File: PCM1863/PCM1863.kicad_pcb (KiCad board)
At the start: 2 copper layers, 86 parts, among them IC1 SN74AUC1G126DCKR, IC2 NCP163ASN330T1G, IC3 NCP163ASN330T1G, IC4 TXB0101DBVT, J1 Conn_01x10_Male, J2 Conn_01x10_Male, J3 Conn_01x10_Male, J4 USB_B_Micro, U1 PCM1863, Y1 ASE-24.000MHZ-ET, Y2 ASE-22.000MHZ-ET

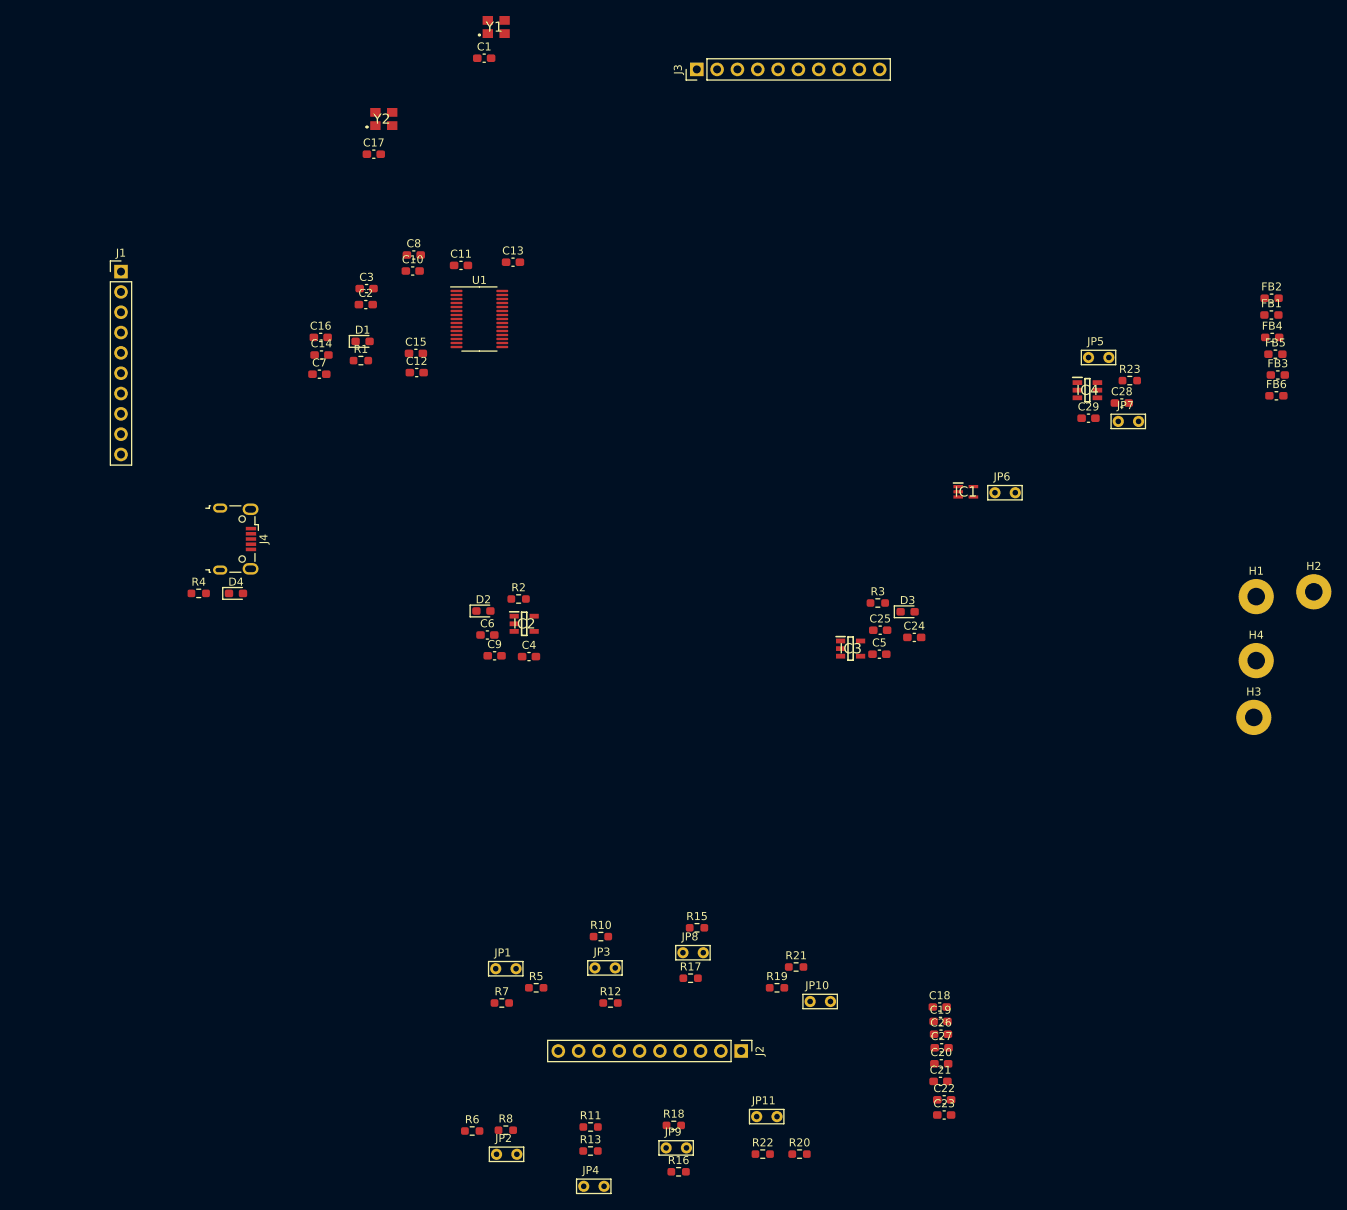
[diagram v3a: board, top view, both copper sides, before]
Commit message: finished ADC v.4
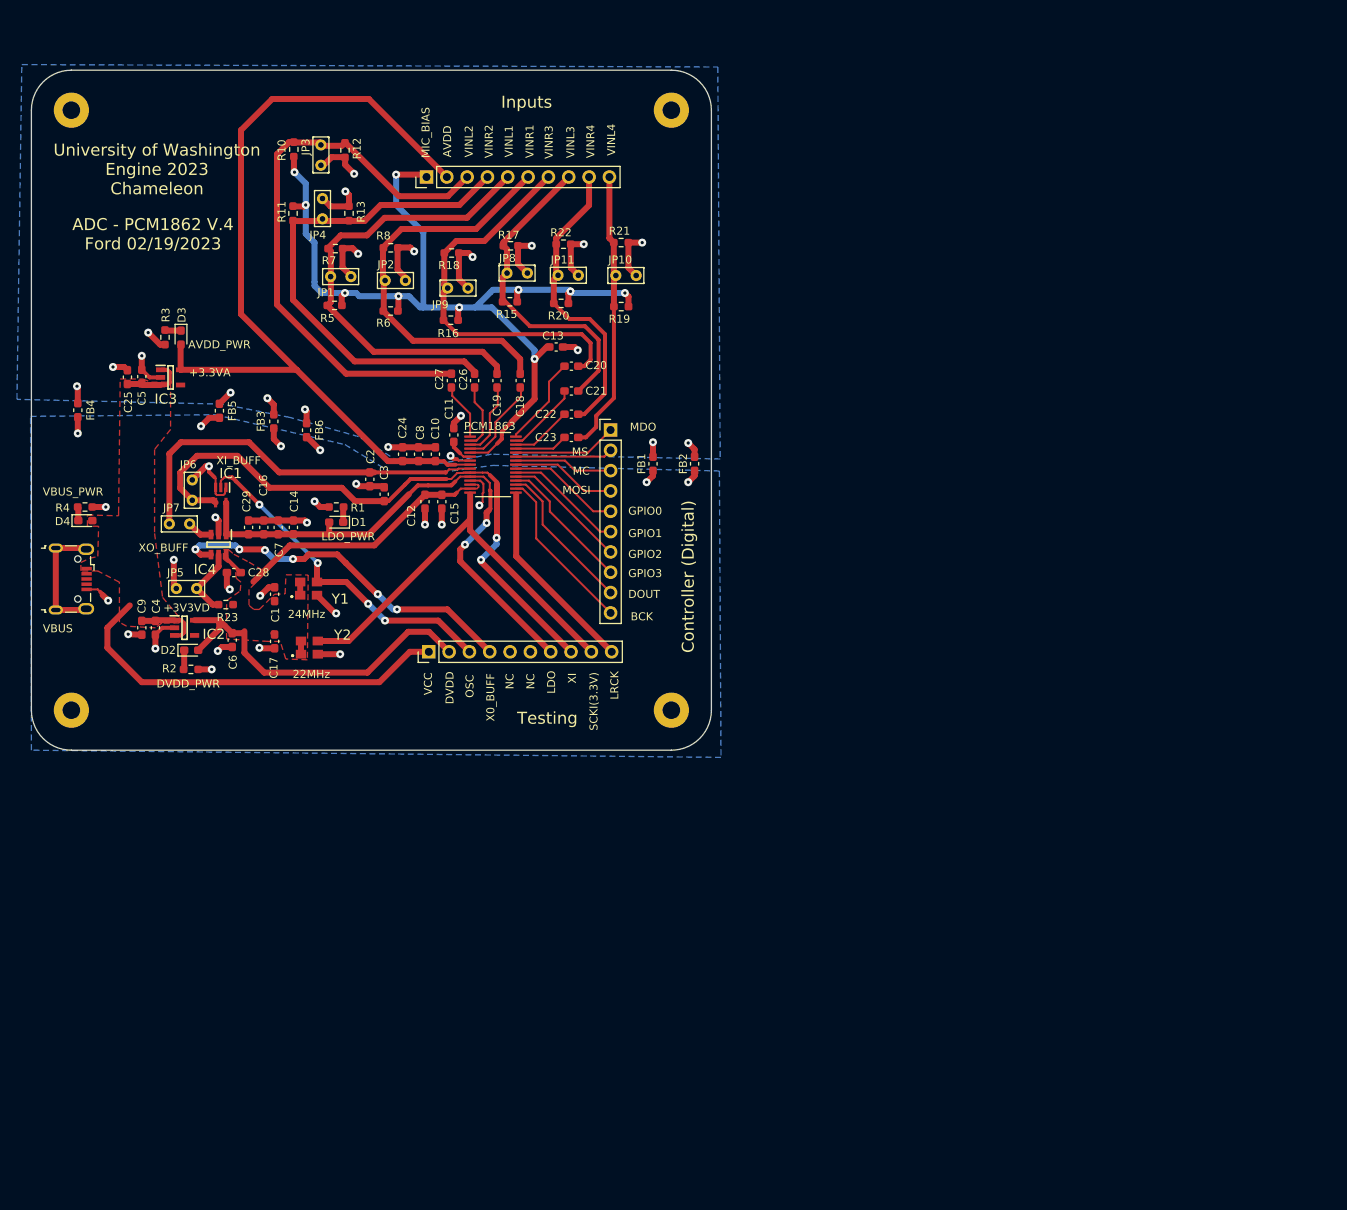
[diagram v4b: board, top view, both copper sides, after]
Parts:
- moved H1 160.1 mm to (75.0, 50.0)
- moved FB4 149.6 mm to (75.8, 87.5), turned to -90 degrees
- moved H3 147.8 mm to (75.0, 125.0)
- moved FB5 132.2 mm to (93.5, 87.6), turned to -90 degrees
- moved JP4 127.1 mm to (107.6, 59.8), turned to -90 degrees
- moved FB3 125.6 mm to (100.3, 88.9), turned to 90 degrees
- moved FB6 121.3 mm to (104.4, 90.0), turned to -90 degrees
- moved R13 121.0 mm to (109.7, 62.9), turned to 90 degrees
- moved R11 120.1 mm to (102.7, 62.9), turned to -90 degrees
- moved JP7 119.3 mm to (86.0, 100.5)
- moved R22 116.4 mm to (136.5, 66.8)
- moved R23 116.4 mm to (94.3, 111.8), turned to 180 degrees
- moved J2 116.1 mm to (119.4, 58.4), turned to 90 degrees
- moved JP5 113.5 mm to (91.9, 111.0), turned to 180 degrees
- moved C28 113.0 mm to (95.3, 107.8), turned to 180 degrees
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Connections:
- C1 pad 2: GND -> GNDD
- C12 pad 2: GND -> GNDD
- C14 pad 2: GND -> GNDD
- C15 pad 2: GND -> GNDD
- C16 pad 2: GND -> GNDD
- C17 pad 2: GND -> GNDD
- C2 pad 1: GND -> GNDD
- C28 pad 2: GND -> GNDD
- C29 pad 1: GND -> GNDD
- C3 pad 1: GND -> GNDD
- C4 pad 2: GND -> GNDD
- C6 pad 1: GND -> GNDD
- C7 pad 2: GND -> GNDD
- C9 pad 2: GND -> GNDD
- FB1 pad 1: GND -> GNDD
- FB2 pad 1: GND -> GNDD
- FB3 pad 1: GND -> GNDD
- FB4 pad 2: GND -> GNDD
- FB5 pad 2: GND -> GNDD
- FB6 pad 2: GND -> GNDD
- H1 pad 1: GND -> GNDA
- H2 pad 1: GND -> GNDA
- H3 pad 1: GND -> GNDD
- H4 pad 1: GND -> GNDD
- IC1 pad 1: GND -> GNDD
- IC1 pad 3: GND -> GNDD
- IC2 pad 2: GND -> GNDD
- IC3 pad 2: GND -> GNDA
- IC4 pad 2: GND -> GNDD
- J1 pad 4: XI -> XO_BUFF
- J1 pad 5: LDO -> unconnected-(J1-Pad5)
- J1 pad 7: unconnected-(J1-Pad7) -> LDO
- J1 pad 8: XO_BUFF -> XI
- J2 pad 1: /1R -> MICBIAS
- J2 pad 10: AVDD -> VINL4
- J2 pad 2: /1L -> AVDD
- J2 pad 3: /2R -> VINL2
- J2 pad 4: /2L -> VINR2
- J2 pad 5: /3R -> VINL1
- J2 pad 6: /3L -> VINR1
- J2 pad 7: /4R -> VINR3
- J2 pad 8: /4L -> VINL3
- J2 pad 9: MICBIAS -> VINR4
- J3 pad 1: BCK -> /MDO
- J3 pad 10: /INT/GPIO3/INTC -> BCK
- J3 pad 2: DOUT -> /MD1/MS/AD
- J3 pad 3: /MDO -> /MD3/MC/SCL
- J3 pad 4: /MD1/MS/AD -> /DOUT2/MD2/MOSI/SDA
- J3 pad 5: /MD3/MC/SCL -> /MD4/MISO/GPIO0
- J3 pad 6: /DOUT2/MD2/MOSI/SDA -> /MD5/GPIO1/INTA/DMIN
- J3 pad 7: /MD4/MISO/GPIO0 -> /MD6/GPIO2/INTB/DMCLK
- J3 pad 8: /MD5/GPIO1/INTA/DMIN -> /INT/GPIO3/INTC
- J3 pad 9: /MD6/GPIO2/INTB/DMCLK -> DOUT
- J4 pad 5: GNDA -> GNDD
- JP5 pad 2: GND -> GNDD
- JP6 pad 2: GND -> GNDD
- R1 pad 2: GND -> GNDD
- R2 pad 2: GND -> GNDD
- R4 pad 1: GNDA -> GNDD
- U1 pad 12: GND -> GNDD
- Y1 pad 2: GND -> GNDD
- Y2 pad 2: GND -> GNDD
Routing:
- net MICBIAS: track 0.00 -> 121.5 mm, vias 0 -> 10
- net AVDD: track 0.00 -> 108.4 mm
- net DVDD: track 0.00 -> 84.8 mm
- net GNDA: track 0.00 -> 83.2 mm, vias 0 -> 21
- net XI: track 0.00 -> 78.6 mm, vias 0 -> 2
- net GNDD: track 0.00 -> 77.2 mm, vias 0 -> 26
- net VINL2: track 0.00 -> 72.7 mm
- net LDO: track 0.00 -> 69.2 mm, vias 0 -> 2
- net VCC: track 0.00 -> 66.1 mm
- net VINR2: track 0.00 -> 63.4 mm
- net VINL1: track 0.00 -> 59.0 mm
- net VINR1: track 0.00 -> 51.4 mm
- net SCKI(3.3V): track 0.00 -> 51.3 mm
- net XO: track 0.00 -> 49.3 mm
- net VINR3: track 0.00 -> 49.3 mm
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- added copper zone on F.Cu, net DVDD
- added copper zone on B.Cu, net GNDA
- added copper zone on B.Cu, net GNDD
- added copper zone on F.Cu, net VCC
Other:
- board outline added: 85 x 85 mm
- board text added: "+3.3VA"
- board text added: "+3V3VD"
- board text added: "22MHz"
- board text added: "24MHz"
- board text added: "ADC - PCM1862 V.4 Ford 02/19/2023"
- board text added: "AVDD"
- board text added: "AVDD_PWR"
- board text added: "BCK"
- board text added: "Controller (Digital)"
- board text added: "DOUT"
- board text added: "DVDD"
- board text added: "DVDD_PWR"
- board text added: "GPIO0"
- board text added: "GPIO1"
- board text added: "GPIO2"
- board text added: "GPIO3"
- board text added: "Inputs"
- board text added: "LDO"
- board text added: "LDO_PWR"
- board text added: "LRCK"
- board text added: "MC"
- board text added: "MDO"
- board text added: "MIC_BIAS"
- board text added: "MOSI"
- board text added: "MS"
- board text added: "NC"
- board text added: "OSC"
- board text added: "PCM1863"
- board text added: "SCKI(3.3V)"
- board text added: "Testing"
- board text added: "University of Washington Engine 2023 Chameleon"
- board text added: "VBUS"
- board text added: "VBUS_PWR"
- board text added: "VCC"
- board text added: "VINL1"
- board text added: "VINL2"
- board text added: "VINL3"
- board text added: "VINL4"
- board text added: "VINR1"
- board text added: "VINR2"
- board text added: "VINR3"
- board text added: "VINR4"
- board text added: "X0_BUFF"
- board text added: "XI"
- board text added: "XI_BUFF"
- board text added: "XO_BUFF"

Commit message: adc update
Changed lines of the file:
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@@
       (pts
         (xy 85 84)
-        (xy 87.4 84)
+        (xy 85 85.7)
         (xy 87.4 89.9)
         (xy 85.4 92.4)
         (xy 85.4 102.9)
         (xy 86.4 110.9)
-        (xy 88.5 113.4)
-        (xy 88.5 114.1)
+        (xy 86.7 113.4)
+        (xy 86.7 114.1)
         (xy 86.3 114.1)
         (xy 85.5 114.7)
